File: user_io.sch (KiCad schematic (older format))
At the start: 1 part

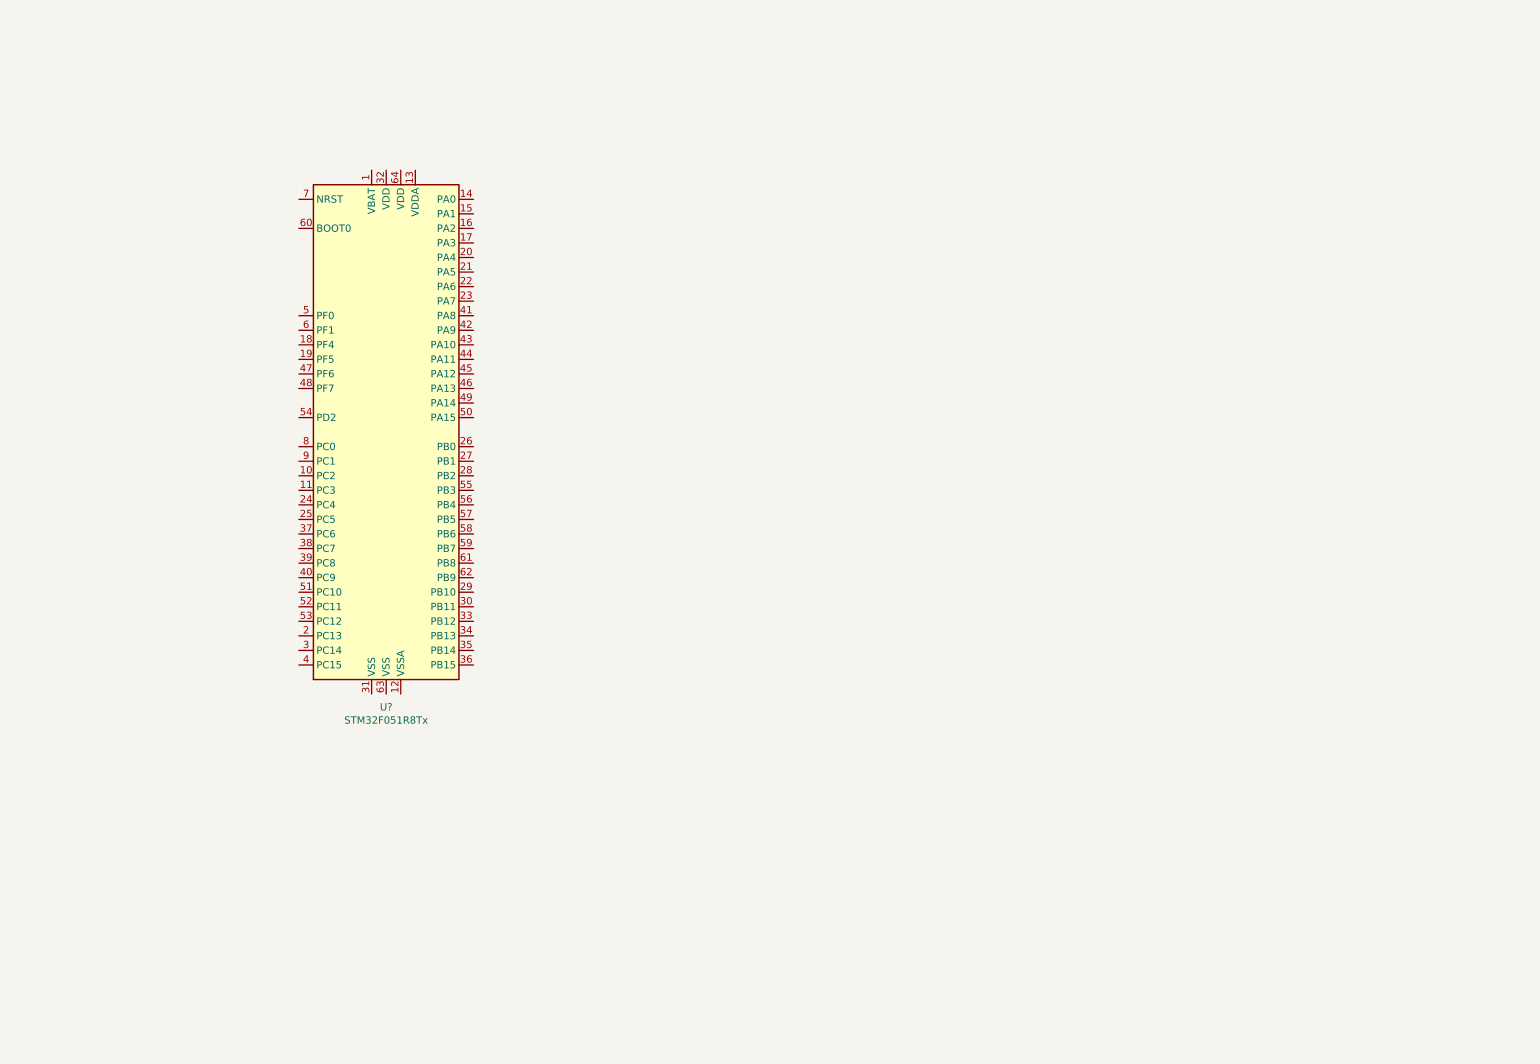
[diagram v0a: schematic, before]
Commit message: Work on user io subsystem schematic
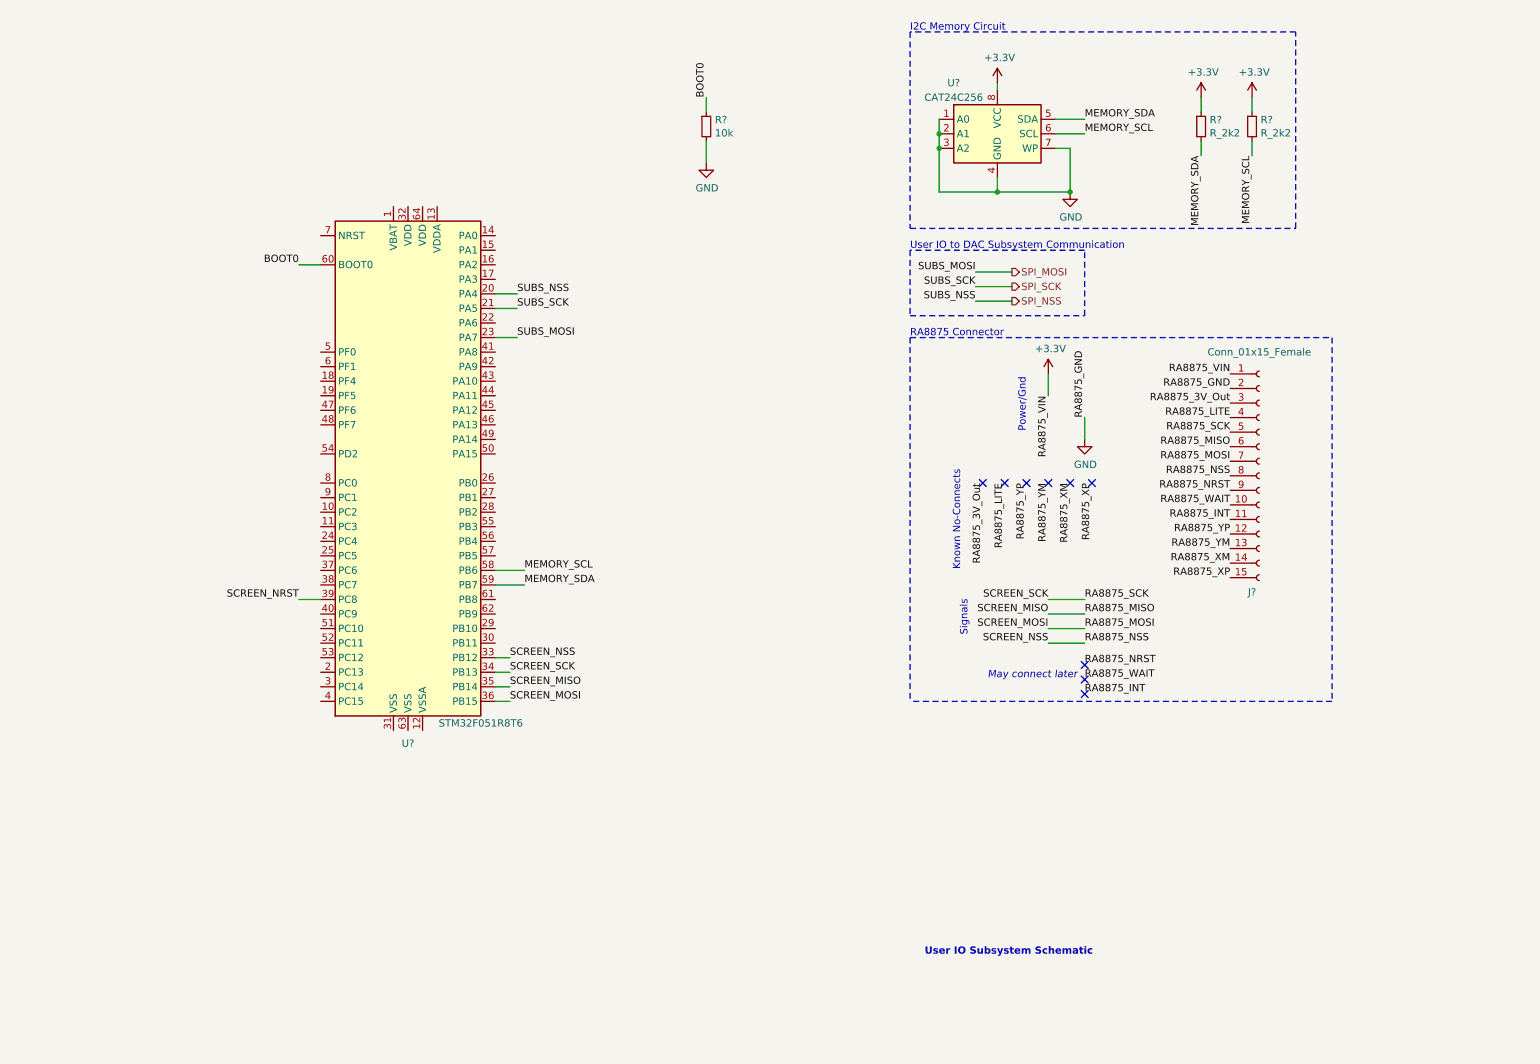
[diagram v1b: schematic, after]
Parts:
- added J?: Conn_01x15_Female, symbol Connector:Conn_01x15_Female
- added R? (x2): R_2k2, symbol Device:R_Small
- added R?: 10k, symbol Device:R_Small
- added U?: CAT24C256, symbol Memory_EEPROM:CAT24C256
- U?: value STM32F051R8Tx -> STM32F051R8T6
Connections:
- net SPI_NSS: now reaches U?.20 (PA4)
- net SPI_SCK: now reaches U?.21 (PA5)
- net SPI_MOSI: now reaches U?.23 (PA7)
- net RA8875_NSS: now reaches U?.33 (PB12)
- net RA8875_NSS: now also J?.8 (Pin_8)
- net RA8875_SCK: now reaches U?.34 (PB13)
- net RA8875_SCK: now also J?.5 (Pin_5)
- net RA8875_MISO: now reaches U?.35 (PB14)
- net RA8875_MISO: now also J?.6 (Pin_6)
- net RA8875_MOSI: now reaches U?.36 (PB15)
- net RA8875_MOSI: now also J?.7 (Pin_7)
- net SCREEN_NRST: now reaches U?.39 (PC8)
- net MEMORY_SCL: now reaches U?.58 (PB6)
- net MEMORY_SCL: now also R?.2, U?.6 (SCL)
- net MEMORY_SDA: now reaches U?.59 (PB7)
- net MEMORY_SDA: now also R?.2, U?.5 (SDA)
- net BOOT0: now reaches U?.60 (BOOT0)
- net BOOT0: now also R?.1
- new net +3V3: J?.1 (Pin_1), R?.1, R?.1, U?.8 (VCC)
- new net GND: J?.2 (Pin_2), R?.2, U?.1 (A0), U?.2 (A1), U?.3 (A2), U?.4 (GND), U?.7 (WP)
- new net RA8875_3V_Out: J?.3 (Pin_3)
- new net RA8875_INT: J?.11 (Pin_11)
- new net RA8875_LITE: J?.4 (Pin_4)
- new net RA8875_NRST: J?.9 (Pin_9)
- new net RA8875_WAIT: J?.10 (Pin_10)
- new net RA8875_XM: J?.14 (Pin_14)
- new net RA8875_XP: J?.15 (Pin_15)
- new net RA8875_YM: J?.13 (Pin_13)
- new net RA8875_YP: J?.12 (Pin_12)
- no-connect marks 0 -> 9
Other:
- note added: "I2C Memory Circuit"
- note added: "Known No-Connects"
- note added: "May connect later"
- note added: "Power/Gnd"
- note added: "RA8875 Connector"
- note added: "Signals"
- note added: "User IO Subsystem Schematic"
- note added: "User IO to DAC Subsystem Communication"
- moved on the sheet: U?

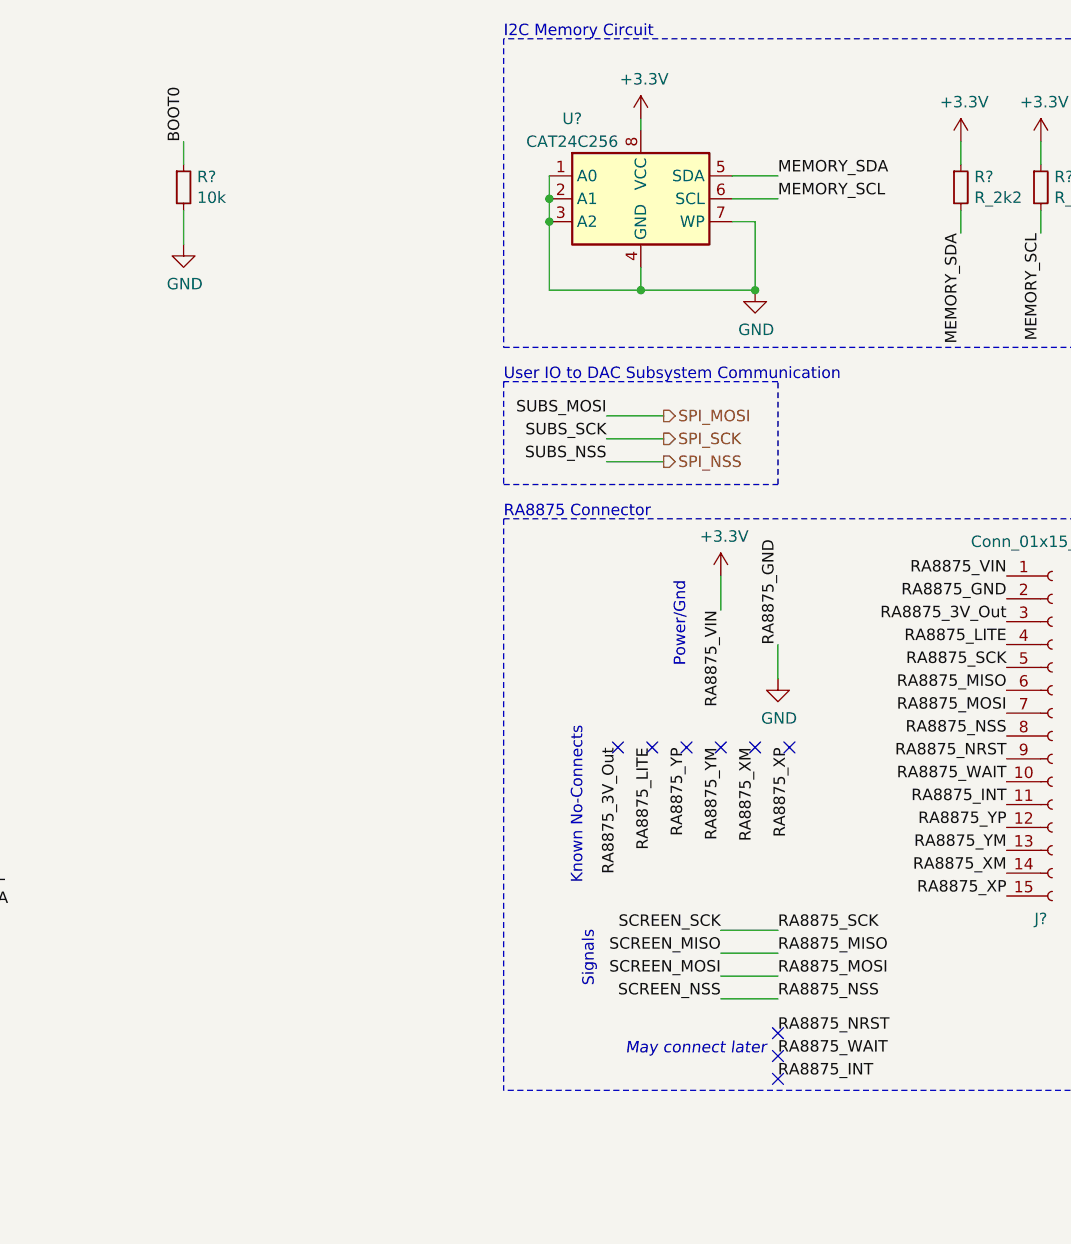
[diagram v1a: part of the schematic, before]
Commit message: Add f4 decoupling capacitors, add dac, add power converter circuit
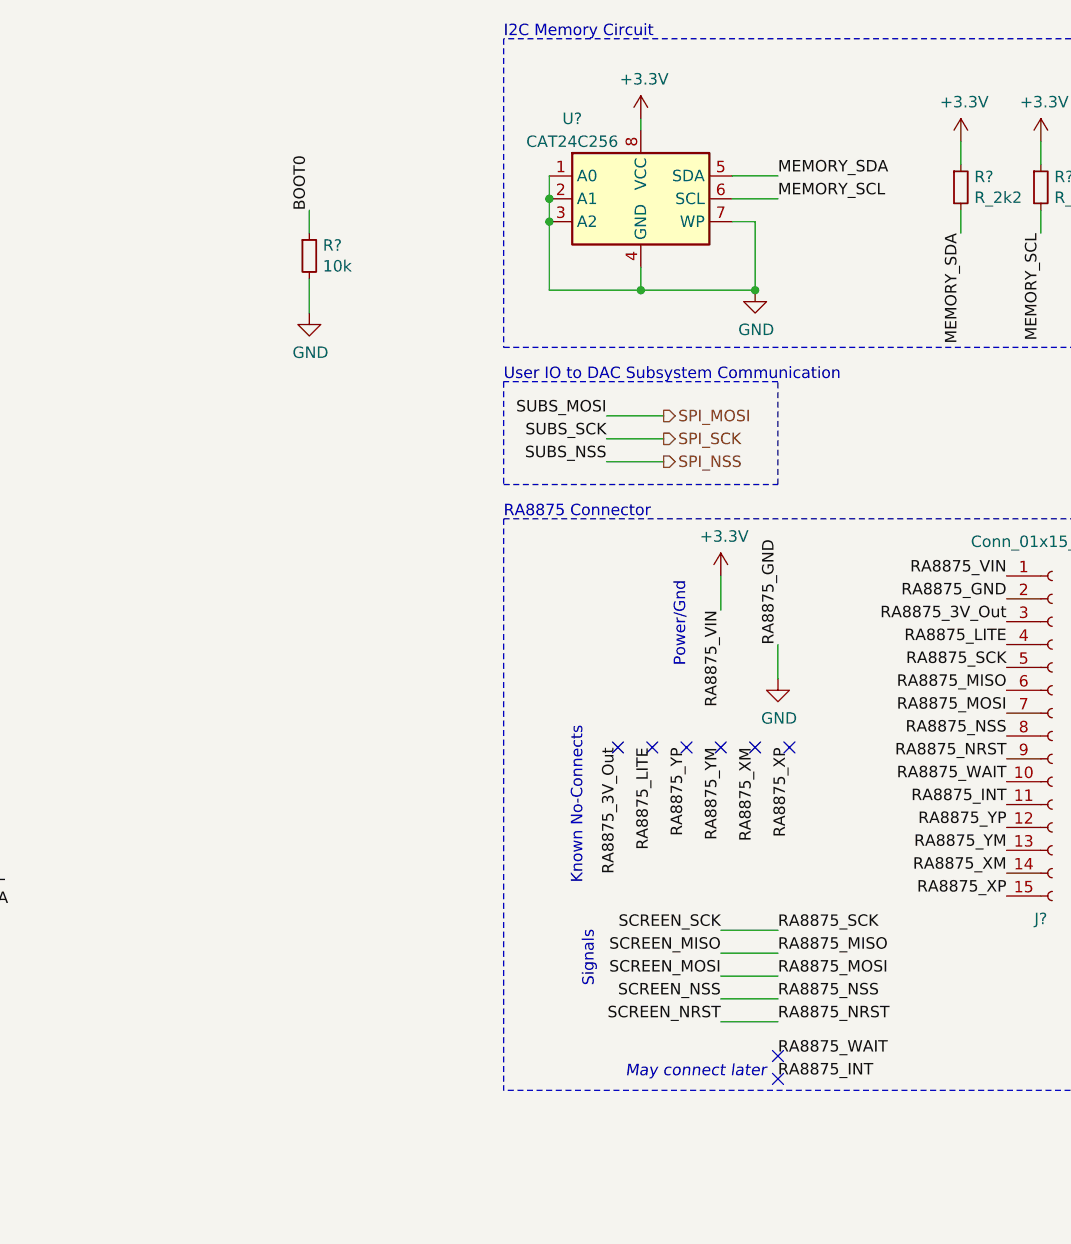
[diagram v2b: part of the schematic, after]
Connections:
- net SCREEN_NRST is gone; now on net RA8875_NRST: U?.39 (PC8)
- no-connect marks 9 -> 8
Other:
- moved on the sheet: R?
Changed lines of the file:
@@
 Text Label 8100 4950 0    50   ~ 0
 RA8875_NSS
-Text Label 8100 5100 0    50   ~ 0
+Text Label 8100 5050 0    50   ~ 0
 RA8875_NRST
 Text Label 8100 5200 0    50   ~ 0
@@
 Wire Wire Line
 	8100 4950 7850 4950
-NoConn ~ 8100 5100
 NoConn ~ 8100 5200
 NoConn ~ 8100 5300
@@
 Text Notes 7300 4900 1    50   ~ 0
 Signals
-Text Notes 8050 5200 2    50   Italic 0
+Text Notes 8050 5300 2    50   Italic 0
 May connect later
 Text Notes 6900 2850 0    50   ~ 0
@@
 Wire Wire Line
 	2700 2350 2850 2350
-Text Label 5500 1200 1    50   ~ 0
+Text Label 6050 1500 1    50   ~ 0
 BOOT0
 $Comp
 L Device:R_Small R?
 U 1 1 605179A2
-P 5500 1400
-F 0 "R?" H 5559 1446 50  0000 L CNN
-F 1 "10k" H 5559 1355 50  0000 L CNN
-F 2 "" H 5500 1400 50  0001 C CNN
-F 3 "~" H 5500 1400 50  0001 C CNN
-	1    5500 1400
+P 6050 1700
+F 0 "R?" H 6109 1746 50  0000 L CNN
+F 1 "10k" H 6109 1655 50  0000 L CNN
+F 2 "" H 6050 1700 50  0001 C CNN
+F 3 "~" H 6050 1700 50  0001 C CNN
+	1    6050 1700
 	1    0    0    -1
 $EndComp
@@
 L power:GND #PWR?
 U 1 1 605180FB
-P 5500 1650
-F 0 "#PWR?" H 5500 1400 50  0001 C CNN
-F 1 "GND" H 5505 1477 50  0000 C CNN
-F 2 "" H 5500 1650 50  0001 C CNN
-F 3 "" H 5500 1650 50  0001 C CNN
-	1    5500 1650
+P 6050 1950
+F 0 "#PWR?" H 6050 1700 50  0001 C CNN
+F 1 "GND" H 6055 1777 50  0000 C CNN
+F 2 "" H 6050 1950 50  0001 C CNN
+F 3 "" H 6050 1950 50  0001 C CNN
+	1    6050 1950
 	1    0    0    -1
 $EndComp
 Wire Wire Line
-	5500 1200 5500 1300
+	6050 1500 6050 1600
 Wire Wire Line
-	5500 1500 5500 1650
+	6050 1800 6050 1950
+Text Label 7850 5050 2    50   ~ 0
+SCREEN_NRST
+Wire Wire Line
+	8100 5050 7850 5050
 $EndSCHEMATC

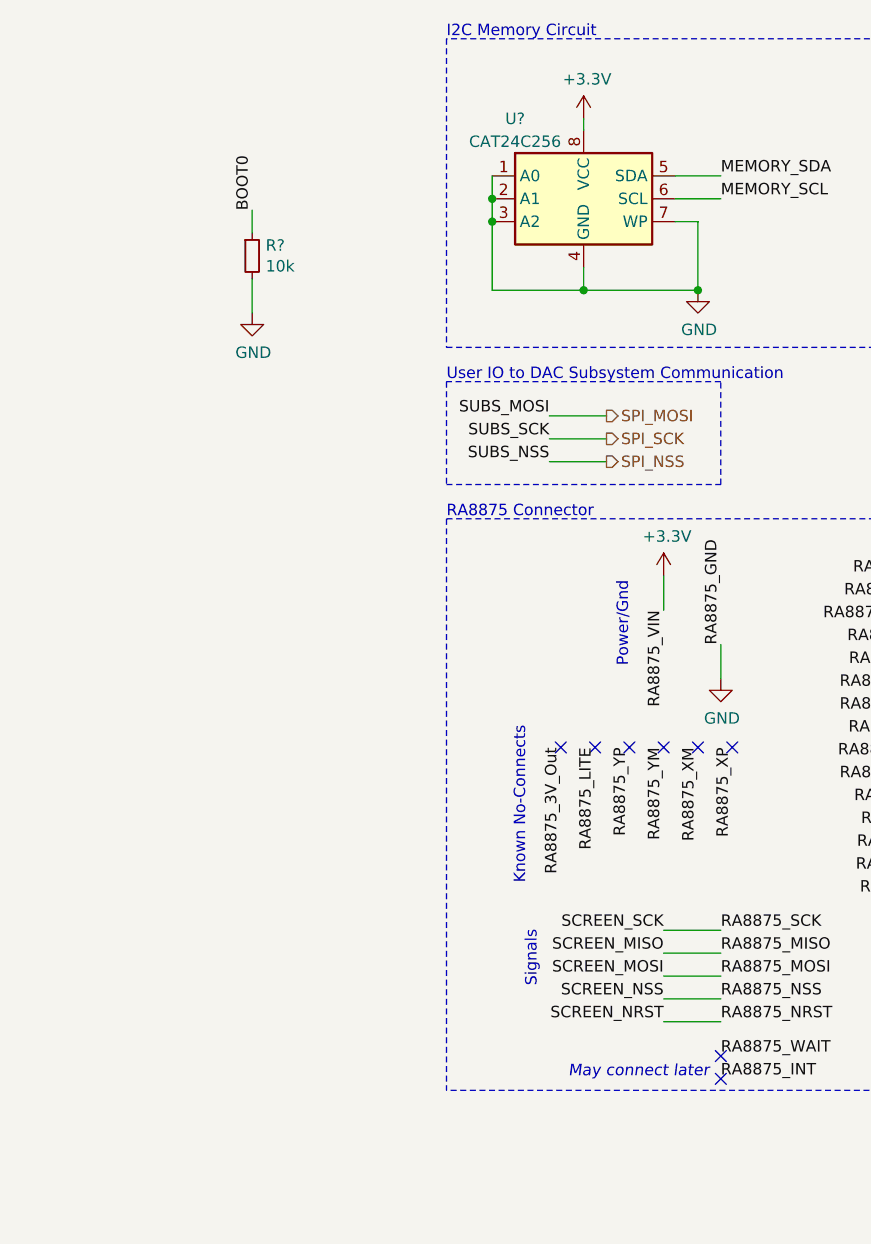
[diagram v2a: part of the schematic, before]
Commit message: Finish prototype of DAC/USB/Power system
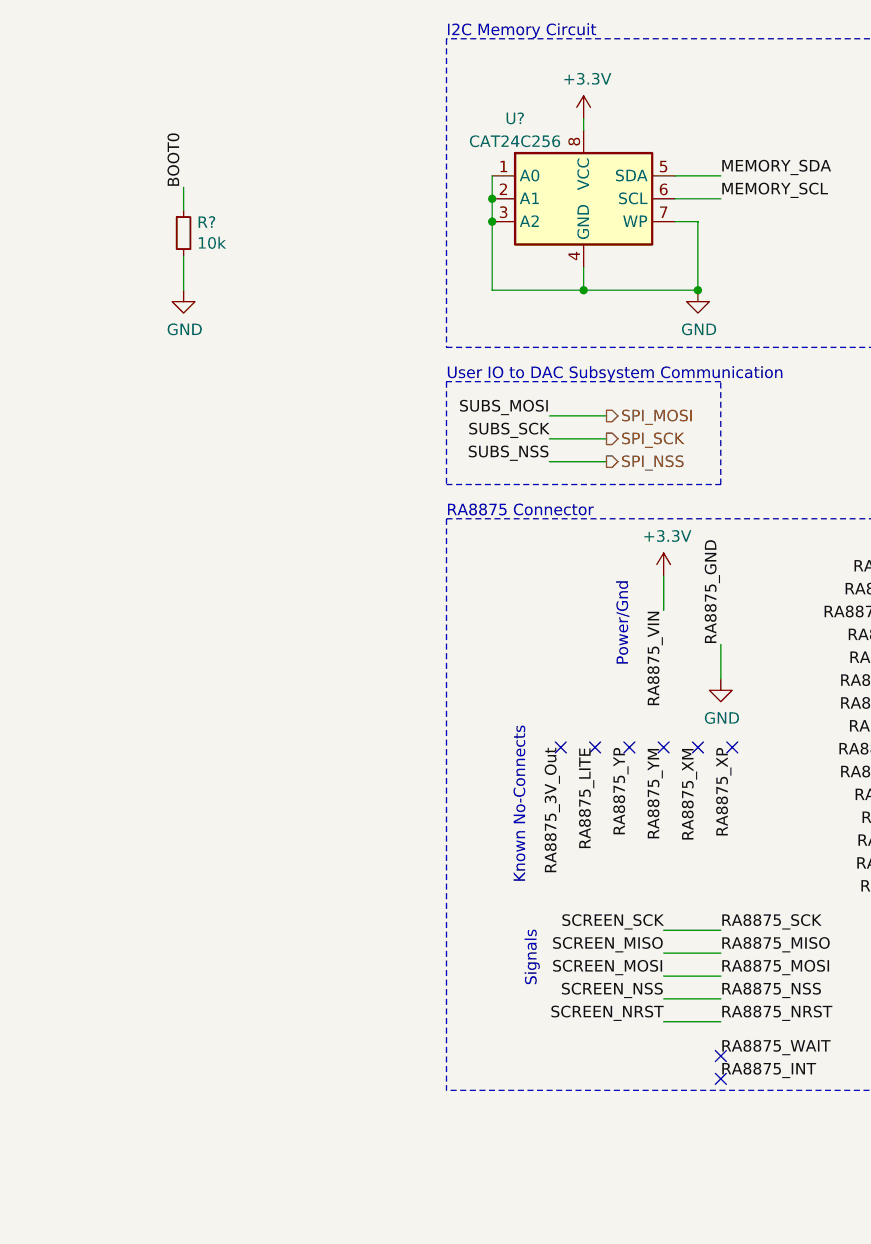
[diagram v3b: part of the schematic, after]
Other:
- note removed: "May connect later"
- moved on the sheet: R?
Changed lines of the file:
@@
 Text Notes 7300 4900 1    50   ~ 0
 Signals
-Text Notes 8050 5300 2    50   Italic 0
-May connect later
 Text Notes 6900 2850 0    50   ~ 0
 RA8875 Connector
@@
 Wire Wire Line
 	2700 2350 2850 2350
-Text Label 6050 1500 1    50   ~ 0
+Text Label 5750 1400 1    50   ~ 0
 BOOT0
 $Comp
 L Device:R_Small R?
 U 1 1 605179A2
-P 6050 1700
-F 0 "R?" H 6109 1746 50  0000 L CNN
-F 1 "10k" H 6109 1655 50  0000 L CNN
-F 2 "" H 6050 1700 50  0001 C CNN
-F 3 "~" H 6050 1700 50  0001 C CNN
-	1    6050 1700
+P 5750 1600
+F 0 "R?" H 5809 1646 50  0000 L CNN
+F 1 "10k" H 5809 1555 50  0000 L CNN
+F 2 "" H 5750 1600 50  0001 C CNN
+F 3 "~" H 5750 1600 50  0001 C CNN
+	1    5750 1600
 	1    0    0    -1
 $EndComp
@@
 L power:GND #PWR?
 U 1 1 605180FB
-P 6050 1950
-F 0 "#PWR?" H 6050 1700 50  0001 C CNN
-F 1 "GND" H 6055 1777 50  0000 C CNN
-F 2 "" H 6050 1950 50  0001 C CNN
-F 3 "" H 6050 1950 50  0001 C CNN
-	1    6050 1950
+P 5750 1850
+F 0 "#PWR?" H 5750 1600 50  0001 C CNN
+F 1 "GND" H 5755 1677 50  0000 C CNN
+F 2 "" H 5750 1850 50  0001 C CNN
+F 3 "" H 5750 1850 50  0001 C CNN
+	1    5750 1850
 	1    0    0    -1
 $EndComp
 Wire Wire Line
-	6050 1500 6050 1600
+	5750 1400 5750 1500
 Wire Wire Line
-	6050 1800 6050 1950
+	5750 1700 5750 1850
 Text Label 7850 5050 2    50   ~ 0
 SCREEN_NRST

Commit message: Finish screen subsystem
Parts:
- added C? (x4): 100n, symbol Device:C_Small
- added C?: 4.7u, symbol Device:C_Small
- added C?: 1u, symbol Device:C_Small
- added C?: 10n, symbol Device:C_Small
- added J?: Conn_01x04, symbol Connector_Generic:Conn_01x04
- added J?: Conn_02x05_Odd_Even, symbol Connector_Generic:Conn_02x05_Odd_Even
- added R?: 10k, symbol Device:R_Small
- added R? (x2): 0, symbol Device:R_Small
- added SW?: SW_DPDT_x2, symbol Switch:SW_DPDT_x2
- added SW?: SW_Push, symbol Switch:SW_Push
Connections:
- net labels added: NRST, SCREEN_INT, SCREEN_WAIT, SWCLK, SWDIO, USART_RX, USART_TX, USR_PUSHBTN, VDDA
- wire segments 38 -> 101
- no-connect marks 8 -> 47
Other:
- note added: "Debug Connector\n"
- note added: "Power Circuit"
- note added: "Reset/Boot Circuitry"
- note added: "USART Debug Connection"
- moved on the sheet: J?, R?, U?
